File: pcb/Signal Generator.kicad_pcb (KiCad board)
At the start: 4 copper layers, 36 x 60 mm, 67 parts, among them J1 AudioJack3, J2 Conn_02x02_Odd_Even, J3 Screw_Terminal_01x04, J4 MEM2080-00-128-00-A, J5 USB_C_Receptacle_USB2.0, J6 Conn_01x04, SW1 SW_Push, SW2 SW_SPDT, U1 FT230XQ, U2 Opamp_Dual, U3 STM32F103RBTx, U4 LD39050PU33R, U5 TLV61048, U6 LDK320AM120R, Y1 TG2520SMN_16.0000M-MCGNNM0

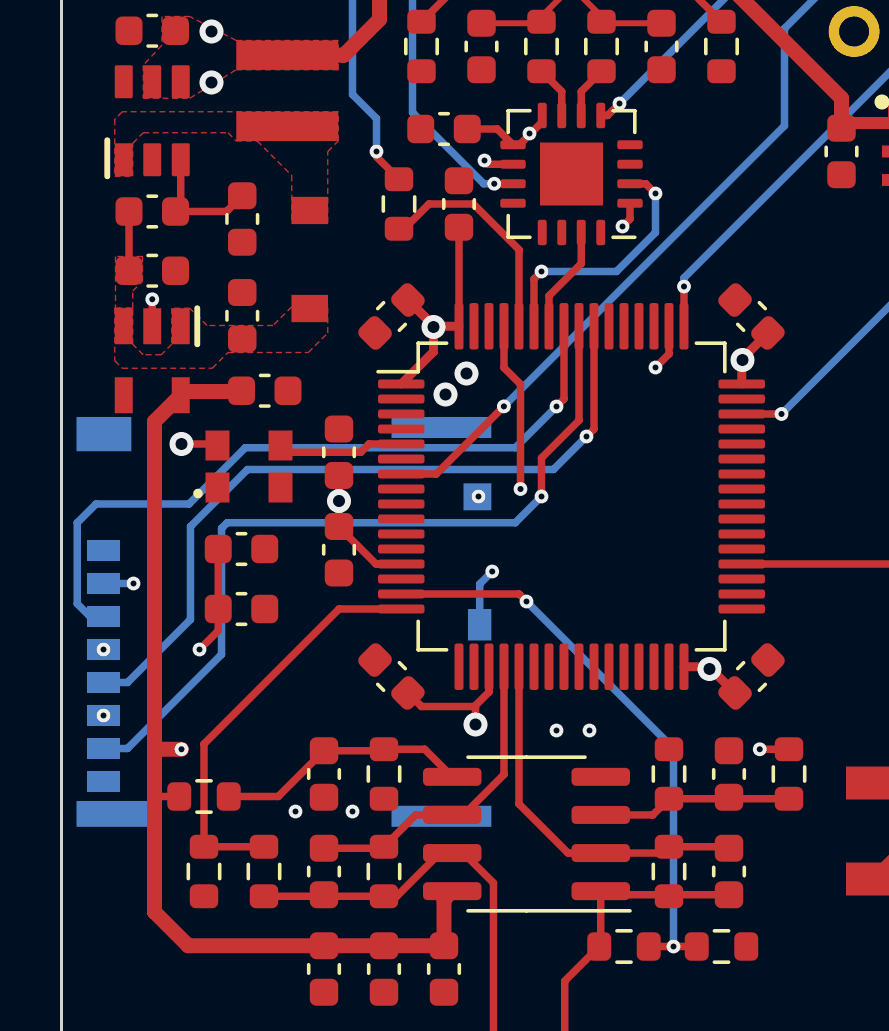
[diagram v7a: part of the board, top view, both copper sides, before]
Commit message: Fixed FTDI connection to the stm32
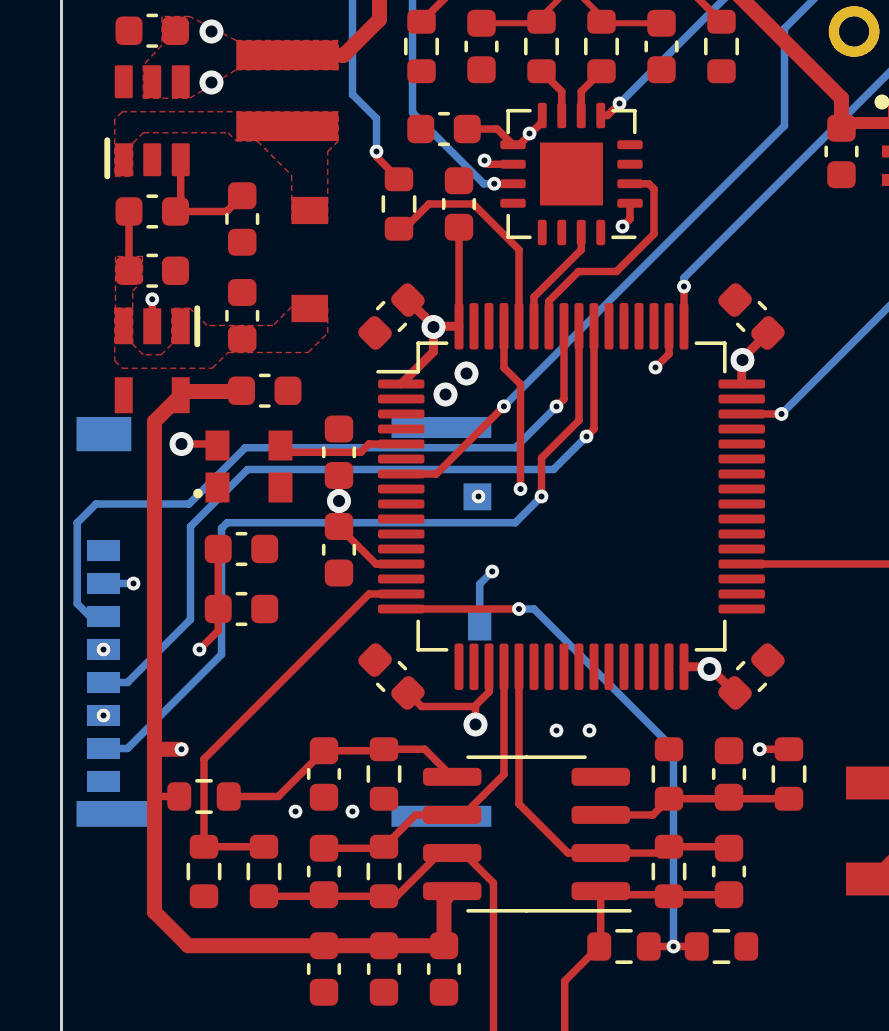
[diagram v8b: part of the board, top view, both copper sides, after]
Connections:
- C7 pad 2: /Output Stage/CH1_OUT -> /Output Stage/CH2_OUT
- C9 pad 2: /Output Stage/CH2_OUT -> /Output Stage/CH1_OUT
- J1 pad R: /Output Stage/CH2_OUT -> /Output Stage/CH1_OUT
- J1 pad T: /Output Stage/CH1_OUT -> /Output Stage/CH2_OUT
- J2 pad 1: /Output Stage/CH1_OUT -> /Output Stage/CH2_OUT
- J2 pad 3: /Output Stage/CH2_OUT -> /Output Stage/CH1_OUT
- J3 pad 1: /Output Stage/CH2_OUT -> /Output Stage/CH1_OUT
- J3 pad 3: /Output Stage/CH1_OUT -> /Output Stage/CH2_OUT
- R11 pad 1: /ADC1 -> /ADC2
- R12 pad 2: /Output Stage/CH2_OUT -> /Output Stage/CH1_OUT
- R14 pad 1: /Output Stage/CH2_OUT -> /Output Stage/CH1_OUT
- R14 pad 2: /ADC2 -> /ADC1
- R16 pad 1: /ADC2 -> /ADC1
- R7 pad 2: /Output Stage/CH1_OUT -> /Output Stage/CH2_OUT
- R9 pad 1: /Output Stage/CH1_OUT -> /Output Stage/CH2_OUT
- R9 pad 2: /ADC1 -> /ADC2
- U1 pad 15: /MCU/UART1_TX -> /MCU/UART1_RX
- U1 pad 2: /MCU/UART1_RX -> /MCU/UART1_TX
- U2 pad 1: /Output Stage/CH1_OUT -> /Output Stage/CH2_OUT
- U2 pad 7: /Output Stage/CH2_OUT -> /Output Stage/CH1_OUT
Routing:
- net /ADC1: track 19.4 -> 13.8 mm, vias 2 -> 0
- net /ADC2: track 13.9 -> 19.2 mm, vias 0 -> 2
- net /MCU/UART1_RX: track 8.55 -> 3.78 mm, vias 2 -> 0
- net /MCU/UART1_TX: track 3.57 -> 7.64 mm
- net /Output Stage/CH2_OUT: track 46.8 -> 43.9 mm
- net /Output Stage/CH1_OUT: track 43.9 -> 46.8 mm
